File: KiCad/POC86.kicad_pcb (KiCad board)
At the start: 2 copper layers, 55 x 116 mm, 4 parts, among them J1 Conn_2Rows-86Pins_even_odd, J2 Conn_2Rows-86Pins_even_odd, J3 Conn_2Rows-86Pins_even_odd

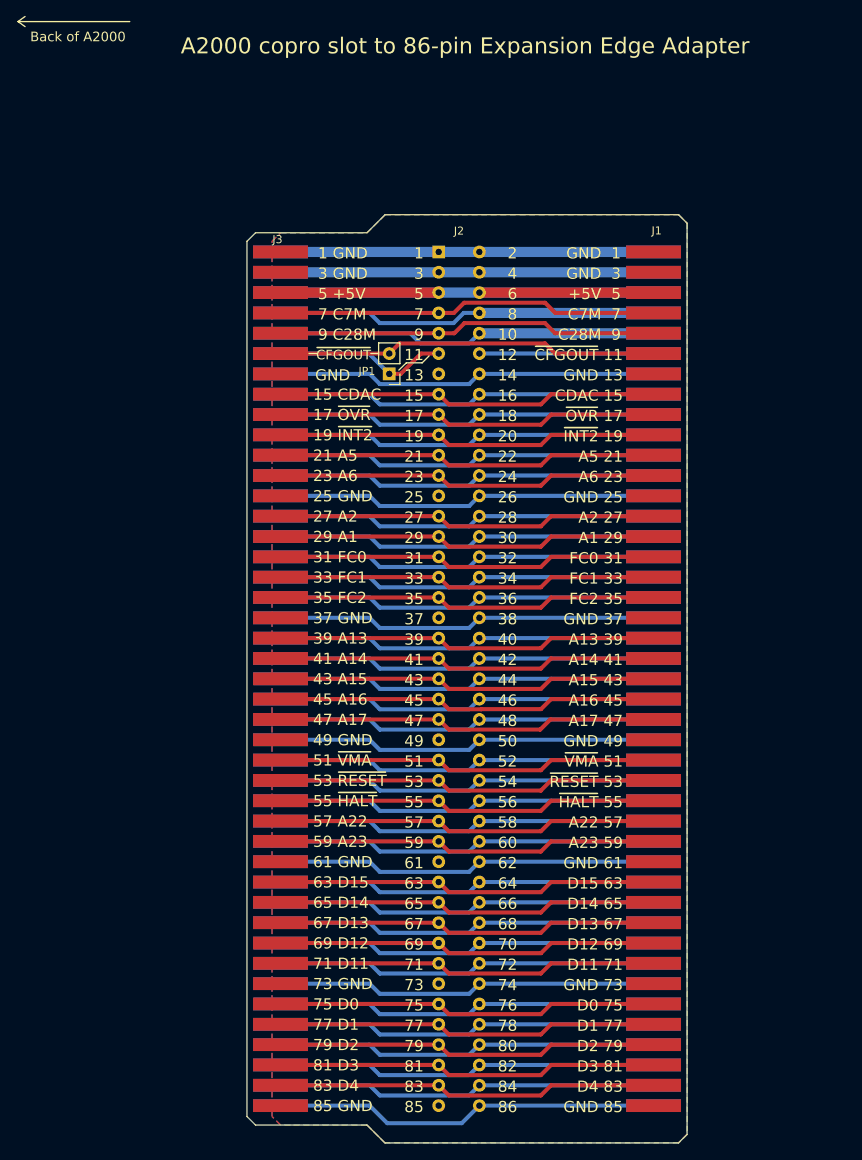
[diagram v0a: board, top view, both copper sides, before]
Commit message: added mounting holes and silkscreen pinout explanations
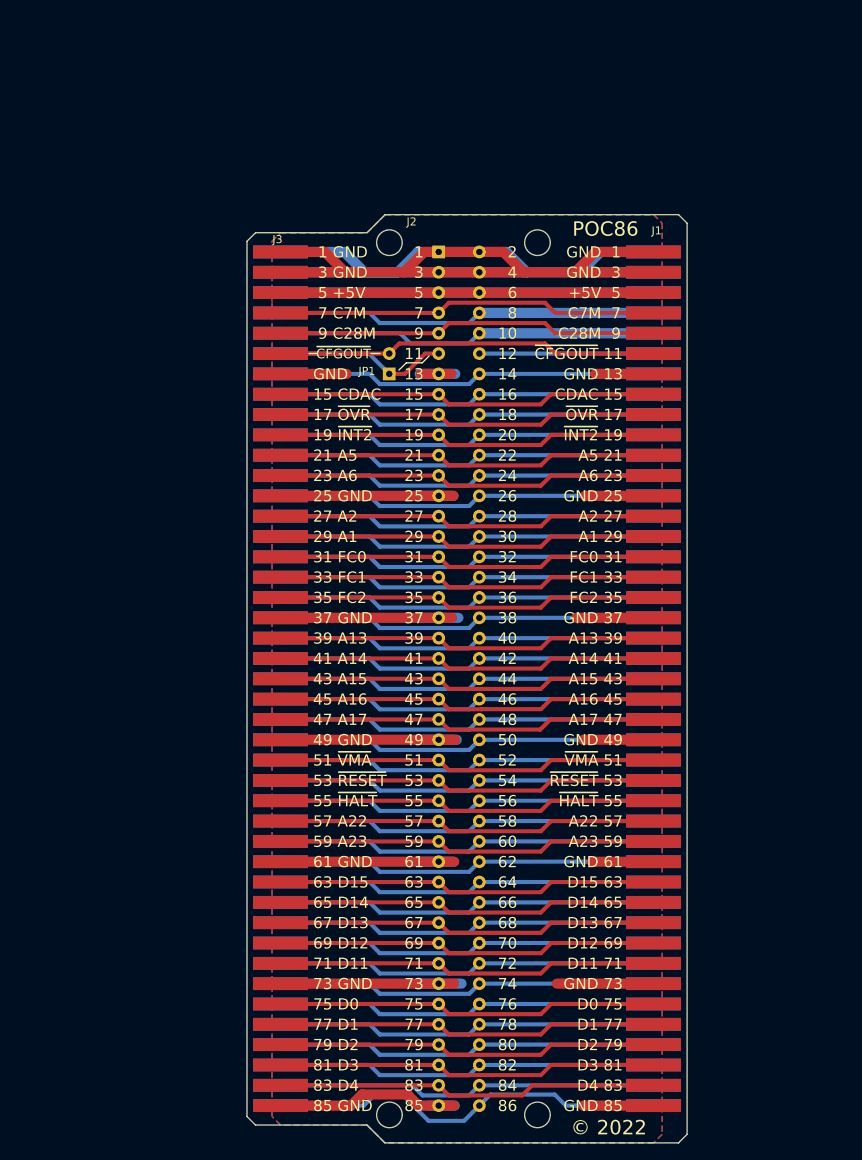
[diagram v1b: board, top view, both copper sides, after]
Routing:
- net GND: track 93.2 -> 411.5 mm
- net +5VDC: track 88.2 -> 93.2 mm
- net D5: track 48.4 -> 50.5 mm
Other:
- outline, holes or cut-outs redrawn
- board text added: "GND 2"
- board text added: "GND 4"
- board text added: "POC86"
- board text added: "© 2022"
- board text removed: "A2000 copro slot to 86-pin Expansion Edge Adapter"
- board text removed: "Back of A2000"

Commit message: added silkscreen on underside of board
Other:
- board text added: "+12V 10"
- board text added: "+5V 6"
- board text added: "-12V 8"
- board text added: "10 +12V"
- board text added: "12 ~CFGIN~"
- board text added: "14 CCKQ"
- board text added: "16 CCK"
- board text added: "18 XRDY"
- board text added: "2 GND"
- board text added: "20 ~BOSS~"
- board text added: "22 ~INT6~"
- board text added: "24 A4"
- board text added: "26 A3"
- board text added: "28 A7"
- board text added: "30 A8"
- board text added: "32 A9"
- board text added: "34 A10"
- board text added: "36 A11"
- board text added: "38 A12"
- board text added: "4 GND"
- board text added: "40 ~IPL0~"
- board text added: "42 ~IPL1~"
- board text added: "44 ~IPL2~"
- board text added: "46 ~BERR~"
- board text added: "48 ~VPA~"
- board text added: "50 E"
- board text added: "52 A18"
- board text added: "54 A19"
- board text added: "56 A20"
- board text added: "58 A21"
- board text added: "6 +5V"
- board text added: "60 ~BR~"
- board text added: "62 ~BGACK~"
- board text added: "64 ~BG~"
- board text added: "66 ~DTACK~"
- board text added: "68 R~W~"
- board text added: "70 ~LDS"
- board text added: "72 ~UDS"
- board text added: "74 ~AS"
- board text added: "76 D10"
- board text added: "78 D9"
- board text added: "8 -12V"
- board text added: "80 D8"
- board text added: "82 D7"
- board text added: "84 D6"
- board text added: "86 D5"
- board text added: "A10 34"
- board text added: "A11 36"
- board text added: "A12 38"
- board text added: "A18 52"
- board text added: "A19 54"
- board text added: "A20 56"
- board text added: "A21 58"
- board text added: "A3 26"
- board text added: "A4 24"
- board text added: "A7 28"
- board text added: "A8 30"
- board text added: "A9 32"
- board text added: "CCK 16"
- board text added: "CCKQ"
- board text added: "D10 76"
- board text added: "D5 86"
- board text added: "D6 84"
- board text added: "D7 82"
- board text added: "D8 80"
- board text added: "D9 78"
- board text added: "E 50"
- board text added: "R~W~ 68"
- board text added: "XRDY 18"
- board text added: "~AS~ 74"
- board text added: "~BERR~ 46"
- board text added: "~BGACK~ 62"
- board text added: "~BG~ 64"
- board text added: "~BOSS~ 20"
- board text added: "~BR~ 60"
- board text added: "~CFGIN"
- board text added: "~DTACK~ 66"
- board text added: "~INT6~ 22"
- board text added: "~IPL0~ 40"
- board text added: "~IPL1~ 42"
- board text added: "~IPL2~ 44"
- board text added: "~LDS~ 70"
- board text added: "~UDS~ 72"
- board text added: "~VPA~ 48"

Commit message: added C1,C2 radial THT-capacitors for +5V-rail
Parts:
- added C1: CP_Small, Capacitor_THT:CP_Radial_D5.0mm_P2.50mm, F.Cu at (116.6, 57.3)
- added C2: CP_Small, Capacitor_THT:CP_Radial_D5.0mm_P2.50mm, F.Cu at (134.1, 57.3)
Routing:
- net +5VDC: track 93.2 -> 106.2 mm
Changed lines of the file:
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@@
   (general
     (thickness 1.6)
-    (drawings 381)
-    (tracks 452)
+    (drawings 382)
+    (tracks 456)
     (zones 0)
-    (modules 4)
+    (modules 6)
     (nets 77)
   )
@@
   )
   (setup
-    (last_trace_width 1.27)
+    (last_trace_width 0.25)
     (user_trace_width 0.2032)
     (user_trace_width 0.254)
@@
     (add_net XRDY)
   )
+  (module Capacitor_THT:CP_Radial_D5.0mm_P2.50mm (layer F.Cu)
+    (at 134.1 57.319 90)
+    (descr "CP, Radial series, Radial, pin pitch=2.50mm, , diameter=5mm, Electrolytic Capacitor")
+    (tags "CP Radial series Radial pin pitch 2.50mm  diameter 5mm Electrolytic Capacitor")
+    (fp_text reference C2 (at -2.2 0.5 180) (layer F.SilkS)
+      (effects (font (size 1 1) (thickness 0.15)))
+    )
+    (fp_text value CP_Small (at 1.25 3.75 90) (layer F.Fab) hide
+      (effects (font (size 1 1) (thickness 0.15)))
+    )
+    (fp_line (start 0 1.2) (end 0 1.8) (layer F.SilkS) (width 0.12))
+    (fp_line (start -0.3 1.5) (end 0.3 1.5) (layer F.SilkS) (width 0.12))
+    (fp_line (start -0.633605 -1.3375) (end -0.633605 -0.8375) (layer F.Fab) (width 0.1))
+    (fp_line (start -0.883605 -1.0875) (end -0.383605 -1.0875) (layer F.Fab) (width 0.1))
+    (fp_circle (center 1.25 0) (end 4 0) (layer F.CrtYd) (width 0.05))
+    (fp_circle (center 1.25 0) (end 3.75 0) (layer F.Fab) (width 0.1))
+    (fp_text user %R (at 1.25 0 90) (layer F.Fab) hide
+      (effects (font (size 1 1) (thickness 0.15)))
+    )
+    (pad 2 thru_hole circle (at 2.5 0 90) (size 1.6 1.6) (drill 0.8) (layers *.Cu *.Mask)
+      (net 1 GND))
+    (pad 1 thru_hole rect (at 0 0 90) (size 1.6 1.6) (drill 0.8) (layers *.Cu *.Mask)
+      (net 4 +5VDC))
+    (model ${KISYS3DMOD}/Capacitor_THT.3dshapes/CP_Radial_D5.0mm_P2.50mm.wrl
+      (at (xyz 0 0 0))
+      (scale (xyz 1 1 1))
+      (rotate (xyz 0 0 0))
+    )
+  )
+  (module Capacitor_THT:CP_Radial_D5.0mm_P2.50mm (layer F.Cu)
+    (at 116.6 57.319 90)
+    (descr "CP, Radial series, Radial, pin pitch=2.50mm, , diameter=5mm, Electrolytic Capacitor")
+    (tags "CP Radial series Radial pin pitch 2.50mm  diameter 5mm Electrolytic Capacitor")
+    (fp_text reference C1 (at -2.2 0.5) (layer F.SilkS)
+      (effects (font (size 1 1) (thickness 0.15)))
+    )
+    (fp_text value CP_Small (at 1.25 3.75 90) (layer F.Fab) hide
+      (effects (font (size 1 1) (thickness 0.15)))
+    )
+    (fp_line (start 0 1.2) (end 0 1.8) (layer F.SilkS) (width 0.12))
+    (fp_line (start -0.3 1.5) (end 0.3 1.5) (layer F.SilkS) (width 0.12))
+    (fp_line (start -0.633605 -1.3375) (end -0.633605 -0.8375) (layer F.Fab) (width 0.1))
+    (fp_line (start -0.883605 -1.0875) (end -0.383605 -1.0875) (layer F.Fab) (width 0.1))
+    (fp_circle (center 1.25 0) (end 4 0) (layer F.CrtYd) (width 0.05))
+    (fp_circle (center 1.25 0) (end 3.75 0) (layer F.Fab) (width 0.1))
+    (fp_text user %R (at 1.25 0 90) (layer F.Fab) hide
+      (effects (font (size 1 1) (thickness 0.15)))
+    )
+    (pad 2 thru_hole circle (at 2.5 0 90) (size 1.6 1.6) (drill 0.8) (layers *.Cu *.Mask)
+      (net 1 GND))
+    (pad 1 thru_hole rect (at 0 0 90) (size 1.6 1.6) (drill 0.8) (layers *.Cu *.Mask)
+      (net 4 +5VDC))
+    (model ${KISYS3DMOD}/Capacitor_THT.3dshapes/CP_Radial_D5.0mm_P2.50mm.wrl
+      (at (xyz 0 0 0))
+      (scale (xyz 1 1 1))
+      (rotate (xyz 0 0 0))
+    )
+  )
   (module Connector_PinHeader_2.54mm:PinHeader_1x02_P2.54mm_Vertical (layer F.Cu)
     (at 116.58 66.81736 180)
@@
     (pad 2 connect rect (at 53.34 -0.381 90) (size 1.6 6.86) (layers B.Cu B.Mask)
       (net 1 GND))
+  )
+  (dimension 18.5 (width 0.15) (layer Dwgs.User)
+    (gr_text "18.500 mm" (at 125.85 44.019) (layer Dwgs.User)
+      (effects (font (size 1 1) (thickness 0.15)))
+    )
+    (feature1 (pts (xy 135.1 50.419) (xy 135.1 44.732579)))
+    (feature2 (pts (xy 116.6 50.419) (xy 116.6 44.732579)))
+    (crossbar (pts (xy 116.6 45.319) (xy 135.1 45.319)))
+    (arrow1a (pts (xy 135.1 45.319) (xy 133.973496 45.905421)))
+    (arrow1b (pts (xy 135.1 45.319) (xy 133.973496 44.732579)))
+    (arrow2a (pts (xy 116.6 45.319) (xy 117.726504 45.905421)))
+    (arrow2b (pts (xy 116.6 45.319) (xy 117.726504 44.732579)))
   )
   (gr_line (start 120.898 65.334) (end 121.533 64.826) (layer F.SilkS) (width 0.12))
@@
   (segment (start 122.76 56.659) (end 127.84 56.659) (width 1.27) (layer B.Cu) (net 4))
   (segment (start 127.84 56.659) (end 122.76 56.659) (width 1.27) (layer F.Cu) (net 4))
+  (segment (start 133.44 56.659) (end 134.1 57.319) (width 0.508) (layer F.Cu) (net 4))
+  (segment (start 127.84 56.659) (end 133.44 56.659) (width 0.508) (layer F.Cu) (net 4))
+  (segment (start 117.26 56.659) (end 116.6 57.319) (width 0.508) (layer F.Cu) (net 4))
+  (segment (start 122.76 56.659) (end 117.26 56.659) (width 0.508) (layer F.Cu) (net 4))
   (segment (start 127.84 97.299) (end 149.6088 97.299) (width 0.508) (layer B.Cu) (net 5))
   (segment (start 126.5691 98.5699) (end 127.84 97.299) (width 0.508) (layer B.Cu) (net 5))
@@
   (segment (start 127.84 59.199) (end 126.57 60.469) (width 0.508) (layer B.Cu) (net 69))
   (segment (start 122.76 59.199) (end 102.991 59.199) (width 0.508) (layer F.Cu) (net 70))
-  (segment (start 137.3182 59.199) (end 149.6088 59.199) (width 0.508) (layer F.Cu) (net 70))
-  (segment (start 136.0491 57.9299) (end 137.3182 59.199) (width 0.508) (layer F.Cu) (net 70))
-  (segment (start 124.0291 57.9299) (end 136.0491 57.9299) (width 0.508) (layer F.Cu) (net 70))
+  (segment (start 131.2582 59.199) (end 149.6088 59.199) (width 0.508) (layer F.Cu) (net 70))
+  (segment (start 129.9891 57.9299) (end 131.2582 59.199) (width 0.508) (layer F.Cu) (net 70))
+  (segment (start 124.0291 57.9299) (end 129.9891 57.9299) (width 0.508) (layer F.Cu) (net 70))
   (segment (start 122.76 59.199) (end 124.0291 57.9299) (width 0.508) (layer F.Cu) (net 70))
   (segment (start 122.76 61.739) (end 102.991 61.739) (width 0.508) (layer F.Cu) (net 71))

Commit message: added Revision to silkscreen print
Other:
- board text added: "Rev. A"

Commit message: added J4-pin on CFGIN-line to easily patch through this signal to J3-edge if J2-slot is empty
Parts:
- added J4: Conn_01x01, Connector_PinHeader_2.54mm:PinHeader_1x01_P2.54mm_Vertical, F.Cu at (134.1, 66.8)
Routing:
- net CFGIN: track 21.8 -> 23.9 mm
- net CCKQ: track 47.7 -> 49.0 mm
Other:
- board text added: "~CFGIN~"

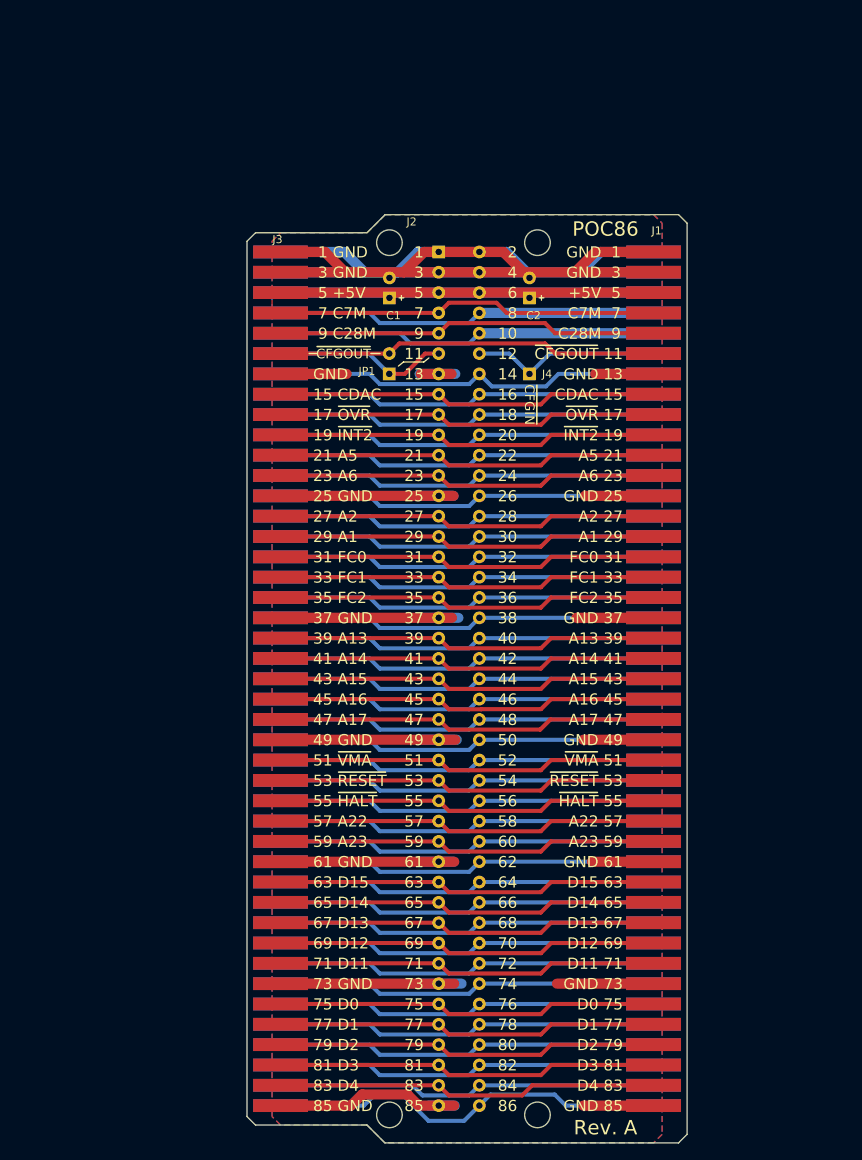
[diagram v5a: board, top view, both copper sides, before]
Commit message: Redesign to a more Compact Edition with no pass-through expansion edge
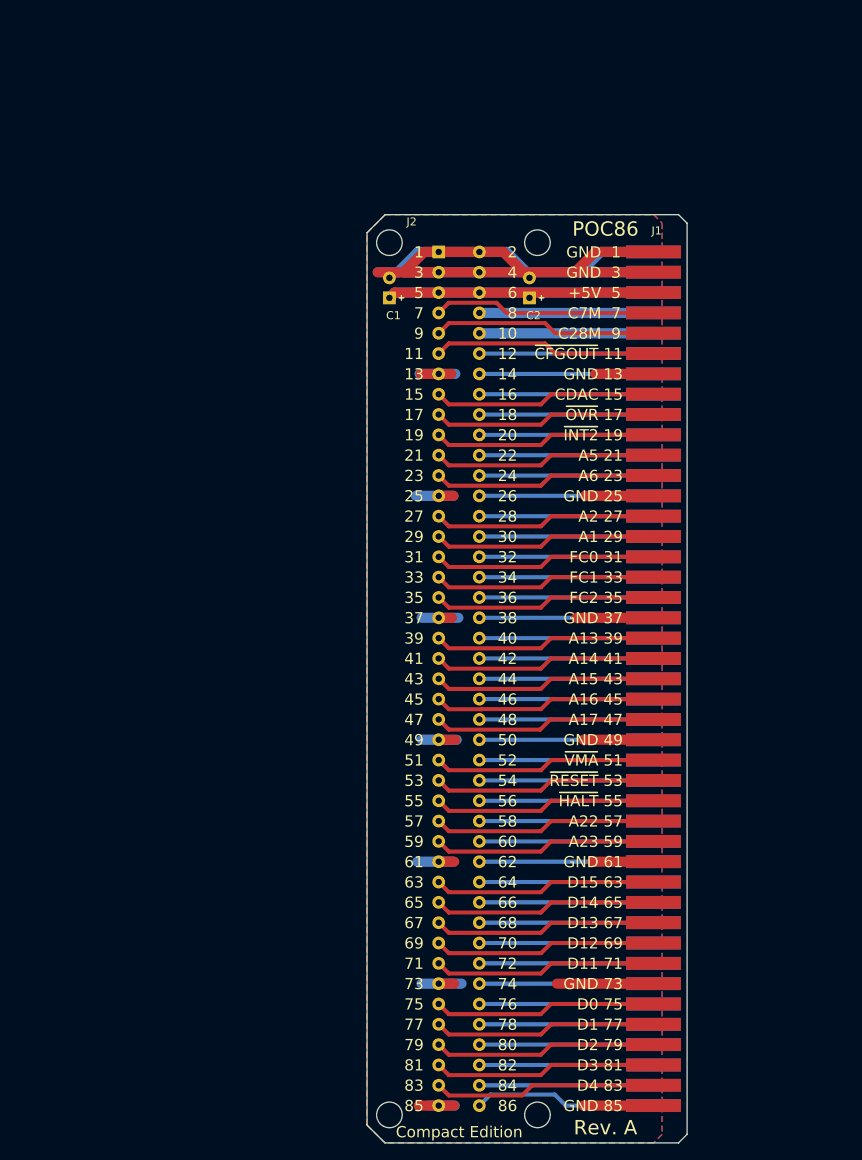
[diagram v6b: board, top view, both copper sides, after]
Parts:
- removed J3: Conn_2Rows-86Pins_even_odd, POC86:A500_86pin_Edge_Connector
- removed J4: Conn_01x01, Connector_PinHeader_2.54mm:PinHeader_1x01_P2.54mm_Vertical
- removed JP1: Jumper_2_Open, Connector_PinHeader_2.54mm:PinHeader_1x02_P2.54mm_Vertical
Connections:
- J2 pad 11: Net-(J2-Pad11) -> CFGOUT
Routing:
- net GND: track 411.5 -> 241.2 mm
- net +5VDC: track 106.2 -> 73.1 mm
- net D5: track 50.5 -> 22.9 mm
- net CCKQ: track 49.0 -> 21.8 mm
- net VPA: track 47.7 -> 21.8 mm
- net RW: track 47.7 -> 21.8 mm
- net LDS: track 47.7 -> 21.8 mm
- net D7: track 47.7 -> 21.8 mm
- net D6: track 47.7 -> 21.8 mm
- net D10: track 47.7 -> 21.8 mm
- net BGACK: track 47.7 -> 21.8 mm
- net BG: track 47.7 -> 21.8 mm
- net A18: track 47.7 -> 21.8 mm
- net A10: track 47.7 -> 21.8 mm
- net D9: track 47.7 -> 21.8 mm
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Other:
- board size 55 x 116 mm -> 40 x 116 mm
- board text added: "Compact Edition"
- board text removed: "+12V 10"
- board text removed: "+5V 6"
- board text removed: "-12V 8"
- board text removed: "1 GND"
- board text removed: "15 CDAC"
- board text removed: "17 ~OVR"
- board text removed: "19 ~INT2"
- board text removed: "21 A5"
- board text removed: "23 A6"
- board text removed: "25 GND"
- board text removed: "27 A2"
- board text removed: "29 A1"
- board text removed: "3 GND"
- board text removed: "31 FC0"
- board text removed: "33 FC1"
- board text removed: "35 FC2"
- board text removed: "37 GND"
- board text removed: "39 A13"
- board text removed: "41 A14"
- board text removed: "43 A15"
- board text removed: "45 A16"
- board text removed: "47 A17"
- board text removed: "49 GND"
- board text removed: "5 +5V"
- board text removed: "51 ~VMA"
- board text removed: "53 ~RESET"
- board text removed: "55 ~HALT"
- board text removed: "57 A22"
- board text removed: "59 A23"
- board text removed: "61 GND"
- board text removed: "63 D15"
- board text removed: "65 D14"
- board text removed: "67 D13"
- board text removed: "69 D12"
- board text removed: "7 C7M"
- board text removed: "71 D11"
- board text removed: "73 GND"
- board text removed: "75 D0"
- board text removed: "77 D1"
- board text removed: "79 D2"
- board text removed: "81 D3"
- board text removed: "83 D4"
- board text removed: "85 GND"
- board text removed: "9 C28M"
- board text removed: "A10 34"
- board text removed: "A11 36"
- board text removed: "A12 38"
- board text removed: "A18 52"
- board text removed: "A19 54"
- board text removed: "A20 56"
- board text removed: "A21 58"
- board text removed: "A3 26"
- board text removed: "A4 24"
- board text removed: "A7 28"
- board text removed: "A8 30"
- board text removed: "A9 32"
- board text removed: "CCK 16"
- board text removed: "CCKQ"
- board text removed: "D10 76"
- board text removed: "D5 86"
- board text removed: "D6 84"
- board text removed: "D7 82"
- board text removed: "D8 80"
- board text removed: "D9 78"
- board text removed: "E 50"
- board text removed: "GND"
- board text removed: "GND 2"
- board text removed: "GND 4"
- board text removed: "R~W~ 68"
- board text removed: "XRDY 18"
- board text removed: "~AS~ 74"
- board text removed: "~BERR~ 46"
- board text removed: "~BGACK~ 62"
- board text removed: "~BG~ 64"
- board text removed: "~BOSS~ 20"
- board text removed: "~BR~ 60"
- board text removed: "~CFGIN"
- board text removed: "~CFGIN~"
- board text removed: "~CFGOUT~"
- board text removed: "~DTACK~ 66"
- board text removed: "~INT6~ 22"
- board text removed: "~IPL0~ 40"
- board text removed: "~IPL1~ 42"
- board text removed: "~IPL2~ 44"
- board text removed: "~LDS~ 70"
- board text removed: "~UDS~ 72"
- board text removed: "~VPA~ 48"
